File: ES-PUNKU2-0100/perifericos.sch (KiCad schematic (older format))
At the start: 38 parts

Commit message: Correcciones al esquemático. Asignación de referencias y valores. Actualización de Librerías.
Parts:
- C10, C8: renamed from C?; footprint (none) -> encapsulados:C_1206_0805_Dual
- C11: renamed from C?; value C -> 100nF; footprint (none) -> encapsulados:C_1206_0805_Dual
- C9: renamed from C?; footprint (none) -> encapsulados:CP_Radial_D10_L20_P5
- D3: renamed from D?; footprint (none) -> encapsulados:DO-214AA
- J10: renamed from J?; footprint (none) -> encapsulados:Bornera_Angulo_3_0.150_Inch
- J11: renamed from J?; footprint (none) -> encapsulados:Pin_Header_Straight_1x04_Pitch2.54mm
- J5, J6, J7: renamed from J?; footprint (none) -> encapsulados:Bornera_Angulo_2_0.150_Inch
- J8: renamed from J?; footprint (none) -> encapsulados:Pin_Header_Straight_1x08_Pitch2.54mm
- J9: renamed from J?; footprint (none) -> encapsulados:Pin_Header_Straight_2x03_Pitch2.54mm
- K1: renamed from K?; footprint (none) -> encapsulados:Relay_NT73_Series_Form_C
- Q1, Q4: renamed from Q?; value BC807 -> BC817; footprint Package_TO_SOT_SMD:SOT-23 -> encapsulados:SOT-23; symbol Transistor_BJT:BC807 -> Transistor_BJT:BC817
- Q2, Q3: renamed from Q?; footprint Package_SO:SOIC-8_3.9x4.9mm_P1.27mm -> encapsulados:SOIC-8
- Q5, Q6, Q7: renamed from Q?; footprint TO_SOT_Packages_SMD:SOT-23 -> encapsulados:SOT-23
- R10, R11, R12, R13, R14, R15, R2, R3, R4, R5, R6, R7, R8, R9: renamed from R?; footprint (none) -> encapsulados:R_1206_0805_Dual
- U5, U6: renamed from U?; footprint DIP-4-SMD -> encapsulados:DIL-8-SMD; DigiKey (none) -> 160-1361-5-ND

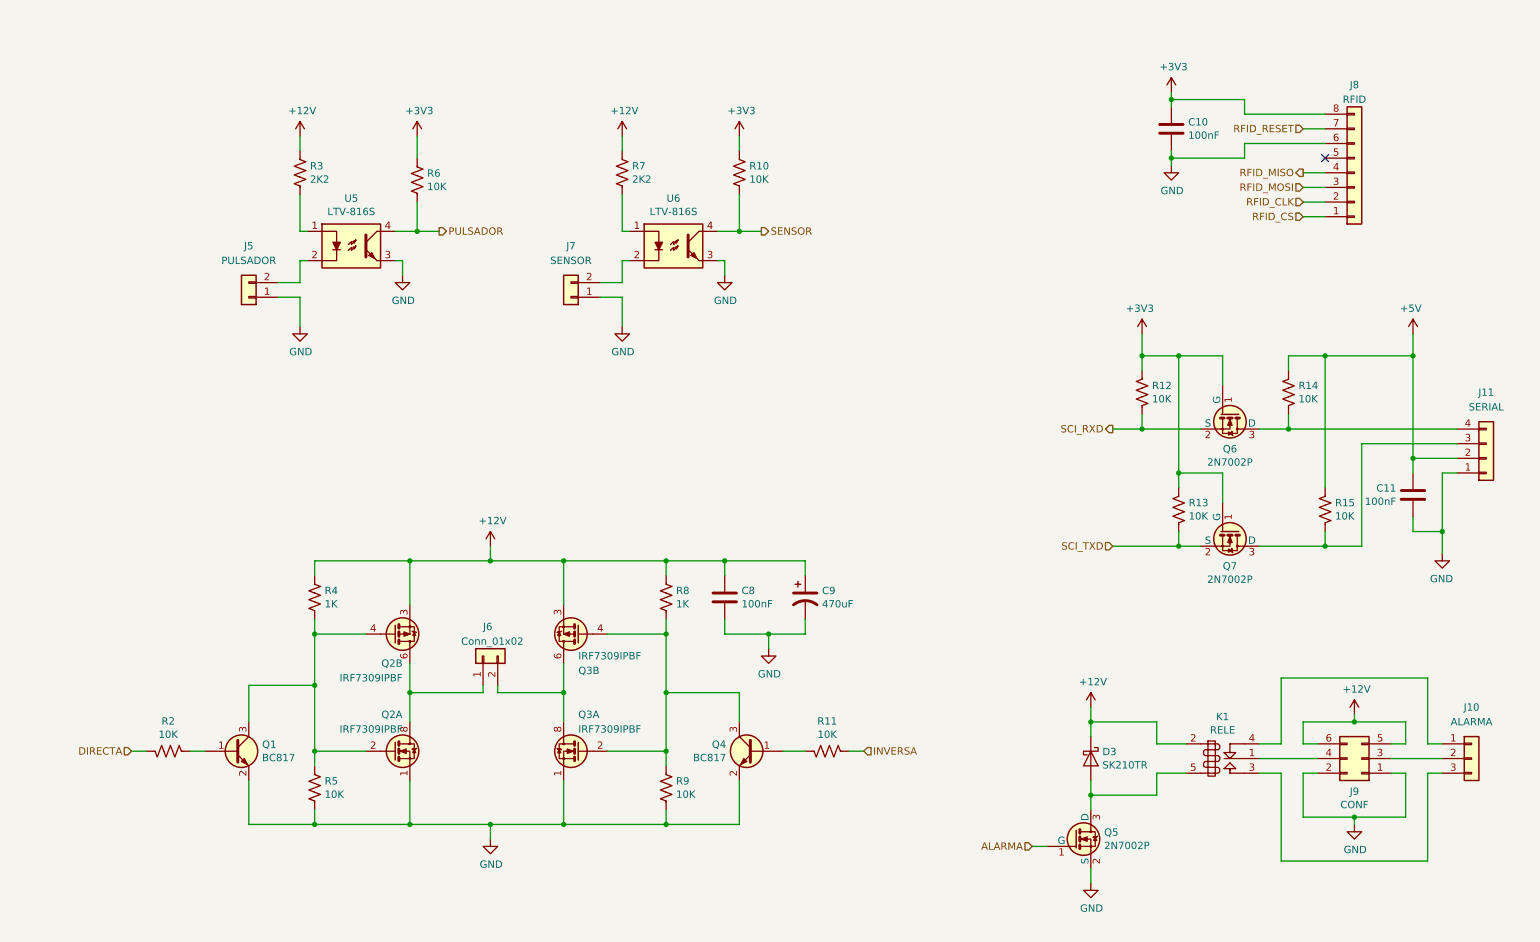
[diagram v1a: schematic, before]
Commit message: Incorporación de las correcciones sugeridas por Martin Ribelotta y posicionamiento de componentes
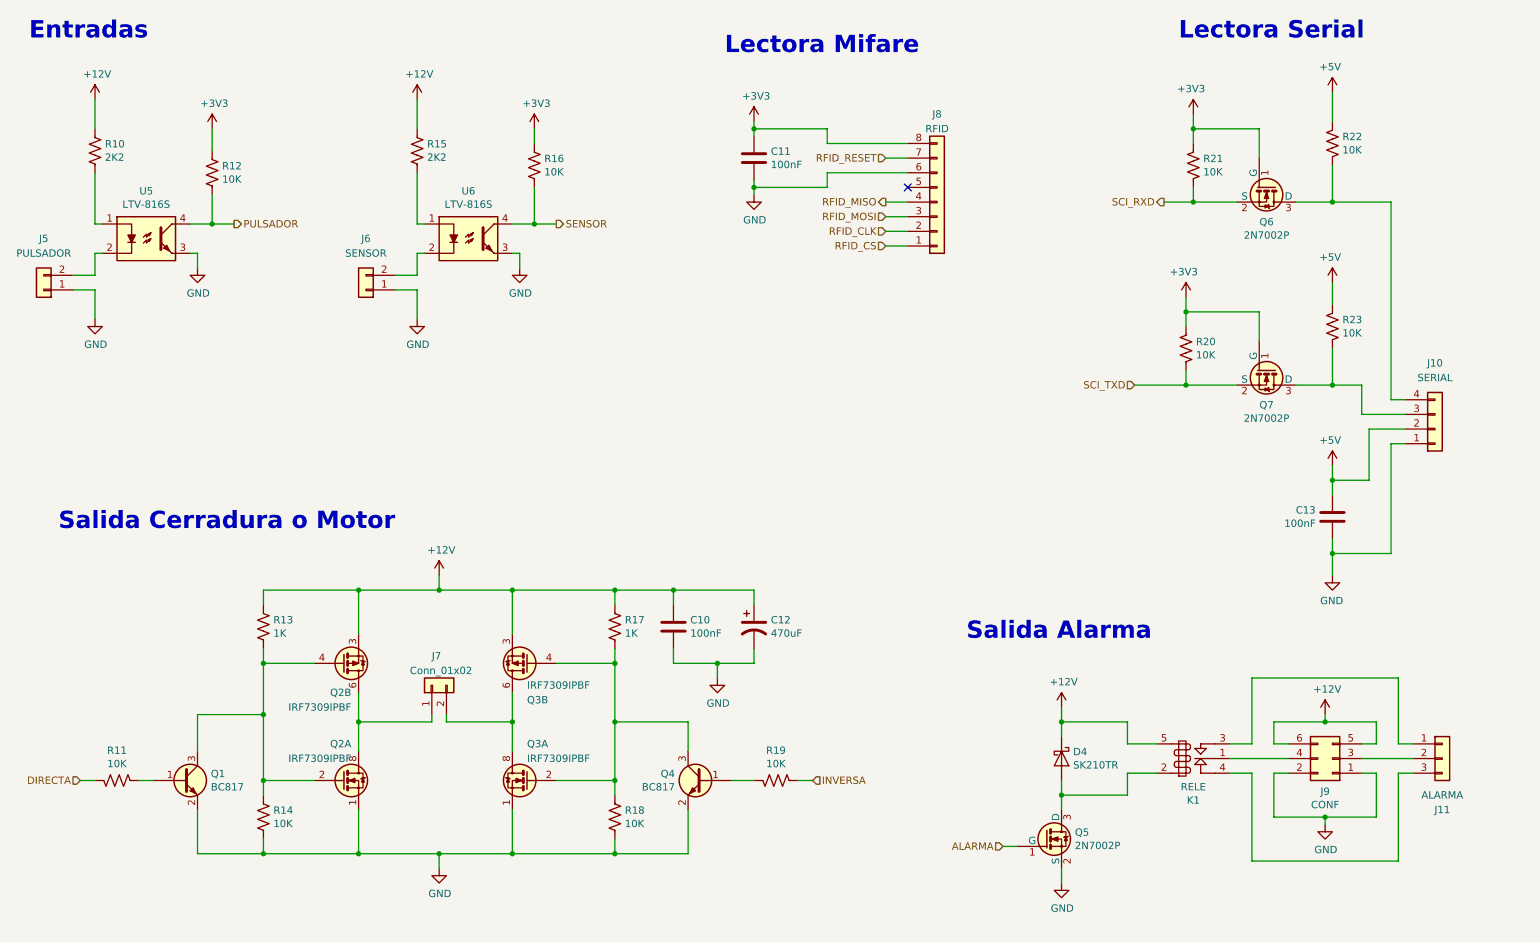
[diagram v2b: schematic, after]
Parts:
- C12: renamed from C9; footprint encapsulados:CP_Radial_D10_L20_P5 -> encapsulados:CP_Elec_8x10
- D4: renamed from D3; Codigo (none) -> SK210TR; Fabricante (none) -> SMC Diode Solutions
- J8: footprint encapsulados:Pin_Header_Straight_1x08_Pitch2.54mm -> encapsulados:PinHeader_2x04_P2.54mm_Vertical_SMD
- K1: footprint encapsulados:Relay_NT73_Series_Form_C -> encapsulados:Relay_NT78_Series_Form_C
- Q1, Q4: Codigo (none) -> BC817,235; DigiKey (none) -> 1727-1978-1-ND; Fabricante (none) -> Nexperia USA Inc.
- Q2, Q3: Codigo (none) -> IRF7309TRPBF; DigiKey (none) -> IRF7309PBFCT-ND; Fabricante (none) -> Infineon Technologies
- Q5, Q6, Q7: Codigo (none) -> 2N7002P,215; DigiKey (none) -> 1727-4692-1-ND; Fabricante (none) -> Nexperia USA Inc.
- U5, U6: Codigo (none) -> LTV-816S; Fabricante (none) -> Lite-On Inc.
- renumbered C8 to C10, C10 to C11, C11 to C13, J11 to J10, J10 to J11, J7 to J6, J6 to J7, R3 to R10, R2 to R11, R6 to R12, R4 to R13, R5 to R14, R7 to R15, R10 to R16, R8 to R17, R9 to R18, R11 to R19, R13 to R20, R12 to R21, R14 to R22, R15 to R23
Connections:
- net +12V: now also K1.5 (B2); no longer K1.2 (B1)
- net at J11.1 (Pin_1): now also K1.3 (NA); no longer K1.4 (NC)
- net at J11.3 (Pin_3): now also K1.4 (NC); no longer K1.3 (NA)
- net at D4.2 (A), Q5.3 (D): now also K1.2 (B1); no longer K1.5 (B2)
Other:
- note added: "Entradas"
- note added: "Lectora Mifare"
- note added: "Lectora Serial"
- note added: "Salida Alarma"
- note added: "Salida Cerradura o Motor"
- moved on the sheet: C10, C11, C12, C13, D4, J10, J11, J5, J6, J7, J8, J9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

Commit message: Primera versión ruteada de la placa
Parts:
- added D5: SK210TR, encapsulados:DO-214AA, symbol Device:D_Schottky
- J7: value Conn_01x02 -> CERRADURA
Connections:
- net +12V: now also D5.1 (K)
- net GND: now also D5.2 (A)
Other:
- moved on the sheet: C10, C11, C12, D4, J11, J5, J6, J8, J9, K1, Q5, R10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

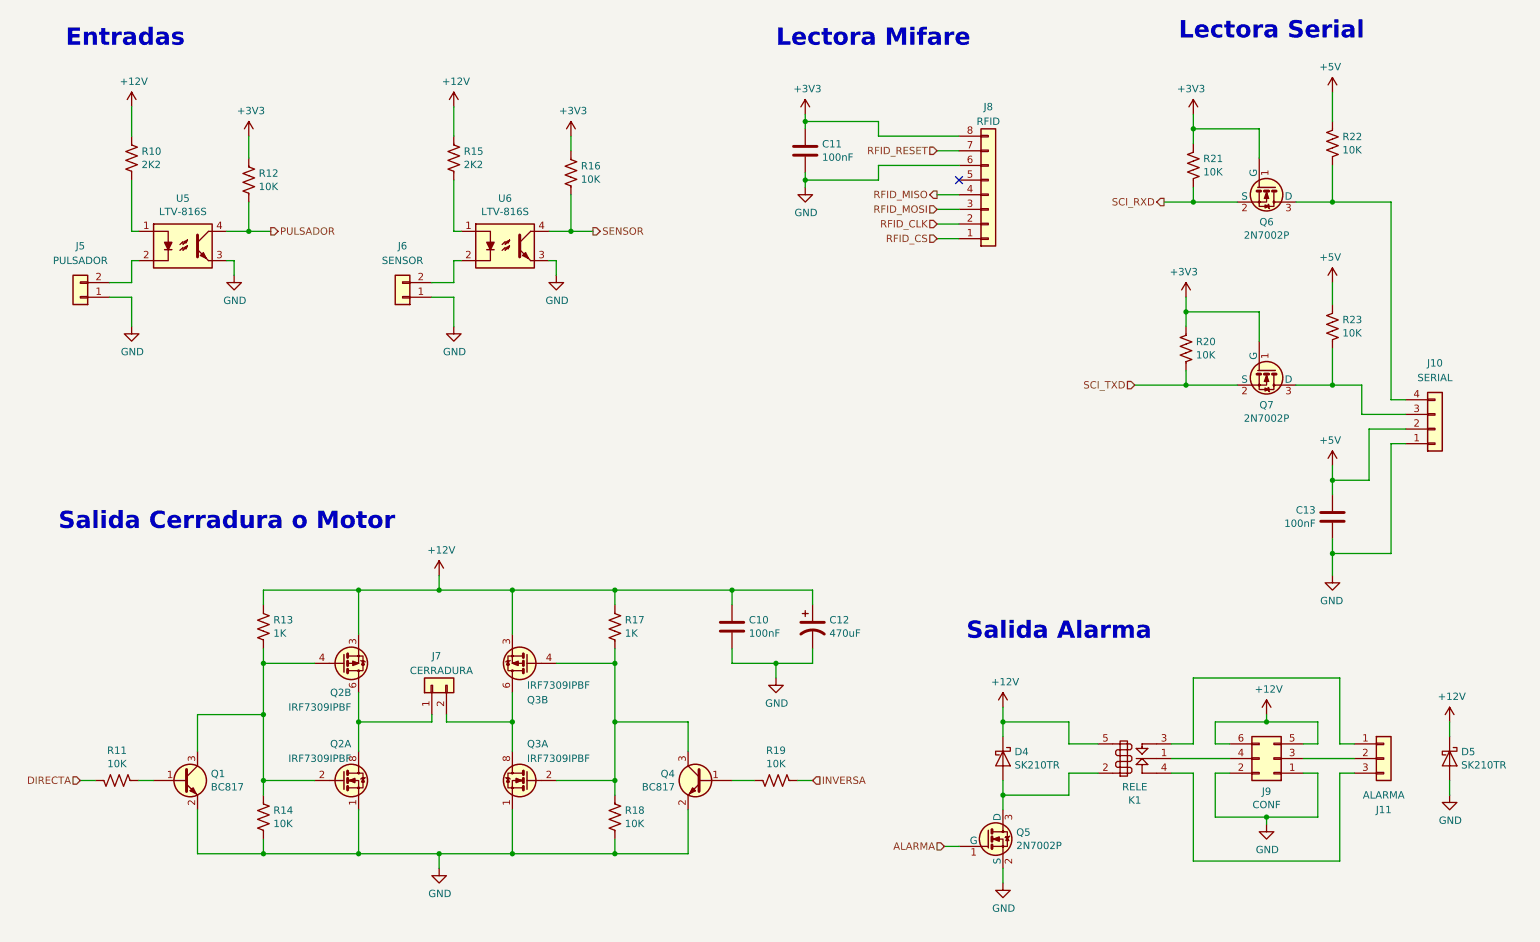
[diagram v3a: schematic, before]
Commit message: Correcciones de ruteo y agregado de una protección para la salida del puente H
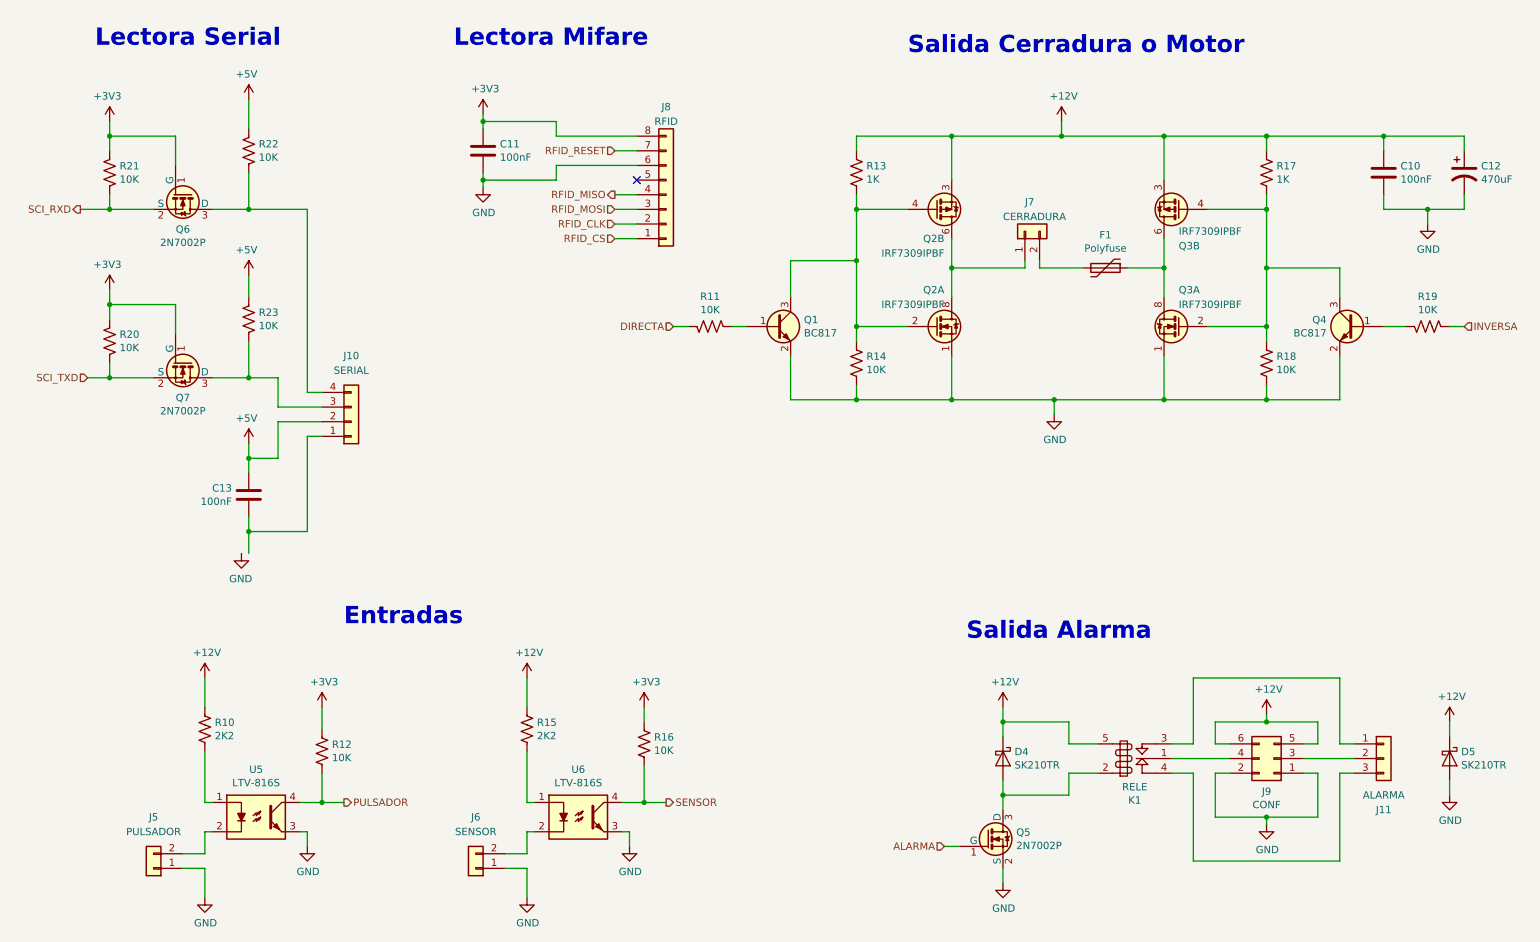
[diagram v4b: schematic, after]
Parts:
- added F1: Polyfuse, Resistor_SMD:R_1812_4532Metric_Pad1.30x3.40mm_HandSolder, symbol Device:Polyfuse
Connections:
- net GND: no longer C13.2, J10.1 (Pin_1)
- net at Q3.5 (D), Q3.6 (D), Q3.7 (D)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: now also F1.1; no longer J7.2 (Pin_2)
- new net: F1.2, J7.2 (Pin_2)
- new net: C13.2, J10.1 (Pin_1)
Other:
- moved on the sheet: C10, C11, C12, C13, J10, J5, J6, J7, J8, Q1, Q2A, Q2B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
